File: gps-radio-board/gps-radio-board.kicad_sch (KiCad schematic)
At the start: 42 parts, among them J1 SMA, J2 SMA, J3 USB_C_Receptacle_USB2.0_16P, J4 JST_BATT, J5 Conn_01x04, J6 Conn_01x04, J7 Conn_01x04, U1 ESP32-C6-MINI-1U-H4, U4 AP2112K-3.3, U5 MAX-M10N, U6 MCP73831, U7 AP2112K-3.3

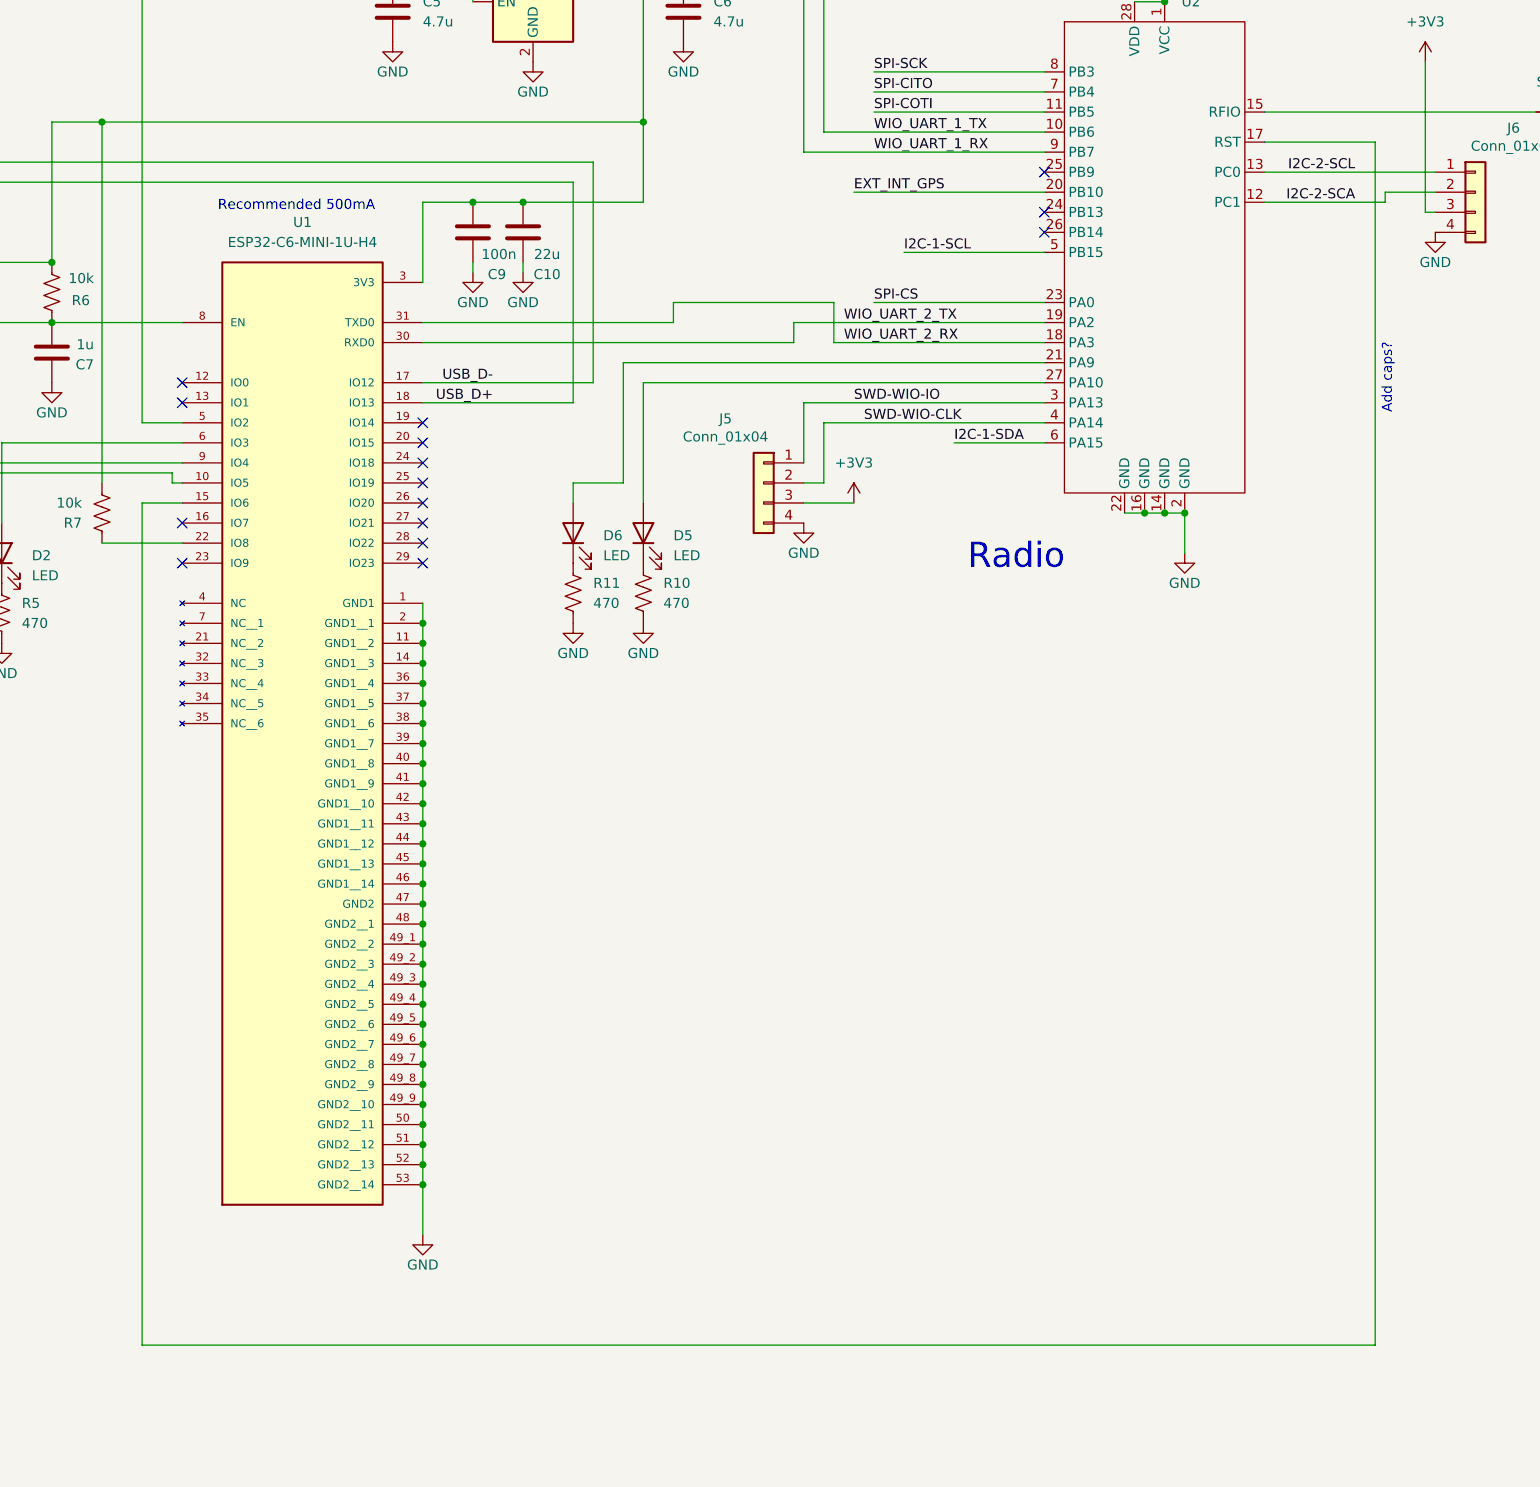
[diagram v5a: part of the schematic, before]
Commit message: Add 3d models for MCUs
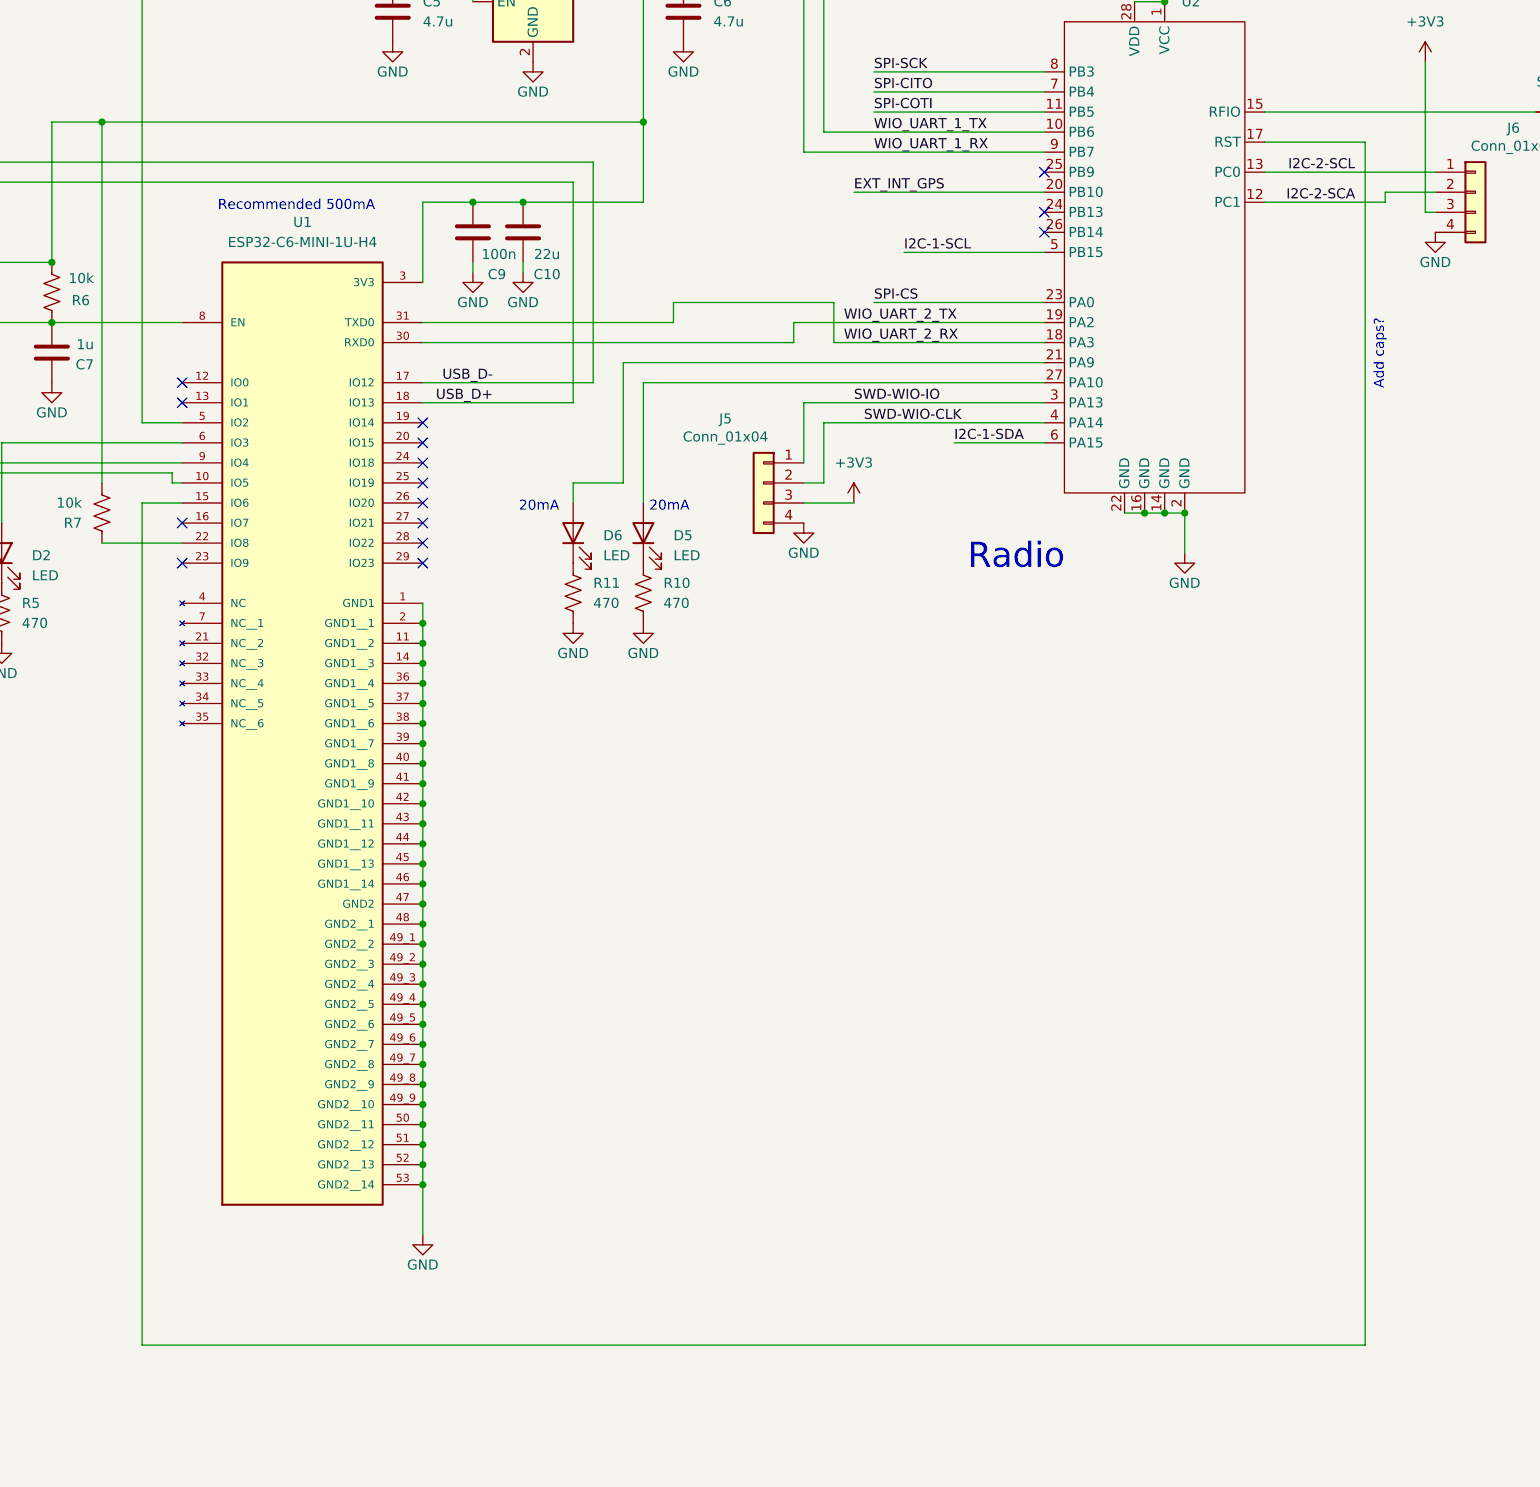
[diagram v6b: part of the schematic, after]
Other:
- note added: "20mA"
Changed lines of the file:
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@@
+		)
+	)
+	(text "20mA"
+		(exclude_from_sim no)
+		(at 558.292 366.268 0)
+		(effects
+			(font
+				(size 1.27 1.27)
+			)
 		)
 	)
@@
 	(text "Add caps?"
 		(exclude_from_sim no)
-		(at 665.734 350.012 90)
+		(at 664.718 346.964 90)
 		(effects
 			(font
@@
 		)
 	)
+	(text "20mA"
+		(exclude_from_sim no)
+		(at 574.802 366.268 0)
+		(effects
+			(font
+				(size 1.27 1.27)
+			)
+		)
+	)
 	(junction
 		(at 543.56 388.62)
@@
 	(wire
 		(pts
-			(xy 664.21 472.44) (xy 664.21 320.04)
+			(xy 662.94 472.44) (xy 662.94 320.04)
 		)
 		(stroke
@@
 	(wire
 		(pts
-			(xy 508 472.44) (xy 664.21 472.44)
+			(xy 508 472.44) (xy 662.94 472.44)
 		)
 		(stroke
@@
 	(wire
 		(pts
-			(xy 664.21 320.04) (xy 650.24 320.04)
-		)
-		(stroke
+			(xy 662.94 320.04) (xy 650.24 320.04)
+		)
+		(stroke

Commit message: Add active gps antenna circuit
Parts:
- added C13, C14: 100n, Capacitor_SMD:C_0603_1608Metric_Pad1.08x0.95mm_HandSolder, symbol Device:C
- added C15: 1u, Capacitor_SMD:C_0603_1608Metric_Pad1.08x0.95mm_HandSolder, symbol Device:C
- added C16: ?, Capacitor_SMD:C_0603_1608Metric_Pad1.08x0.95mm_HandSolder, symbol Device:C
- added L1: ?, Inductor_SMD:L_0603_1608Metric_Pad1.05x0.95mm_HandSolder, symbol Device:L
- added R12: 0, Resistor_SMD:R_0603_1608Metric_Pad0.98x0.95mm_HandSolder, symbol Device:R_US
- added R13, R14: 100k, Resistor_SMD:R_0603_1608Metric_Pad0.98x0.95mm_HandSolder, symbol Device:R_US
- added R15: 10, Resistor_SMD:R_0603_1608Metric_Pad0.98x0.95mm_HandSolder, symbol Device:R_US
- added U3: SiP32431DR3, Package_TO_SOT_SMD:SOT-363_SC-70-6, symbol Power_Management:SiP32431DR3
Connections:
- net +3V3: now also R12.2
- net GND: now also C13.2, C14.2, C15.1, C16.1, R14.1, U3.2 (GND), U3.5 (GND)
- net at C4.1, C5.1, D3.1 (K)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: now also R13.2
- net at J2.1 (In), U5.11 (RF_IN): now also L1.1
- net at U5.13 (LNA_EN): now also U5.14 (VCC_RF), R12.1, R14.2, U3.3 (ON)
- net at U1.5 (IO2), U4.3 (EN): now also R13.1
- net at U1.15 (IO6), U2.17 (RST): now also C13.1
- new net: C16.2, L1.2, R15.2
- new net: C15.2, U3.4 (IN)
- new net: C14.1, R15.1, U3.1 (OUT)
- no-connect marks 24 -> 22
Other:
- note added: "<-Connect if backup supply is wanted"
- note removed: "\/-Connect if backup supply is wanted"
- moved on the sheet: C1, C10, C11, C12, C2, C3, C4, C5, C6, C7, C8, C9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

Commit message: Routing, mostly finished
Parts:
- removed C2: 100n, Capacitor_SMD:C_0603_1608Metric_Pad1.08x0.95mm_HandSolder, symbol Device:C
- removed C3: 10u, Capacitor_SMD:C_0603_1608Metric_Pad1.08x0.95mm_HandSolder, symbol Device:C
- removed R12: 0, Resistor_SMD:R_0603_1608Metric_Pad0.98x0.95mm_HandSolder, symbol Device:R_US
- added BOOT1, GND1: TP2, TestPoint:TestPoint_Pad_1.0x1.0mm, symbol Connector:TestPoint
- added C17: 10u, Capacitor_SMD:C_0603_1608Metric_Pad1.08x0.95mm_HandSolder, symbol Device:C
- added C18: 4.7u, Capacitor_SMD:C_0603_1608Metric_Pad1.08x0.95mm_HandSolder, symbol Device:C
- added C19: 100n, Capacitor_SMD:C_0603_1608Metric_Pad1.08x0.95mm_HandSolder, symbol Device:C
- added EN1, EN2: ESP_EN, TestPoint:TestPoint_Pad_1.0x1.0mm, symbol Connector:TestPoint
- added J8: DM3CS-SF, Connector_Card:microSD_HC_Hirose_DM3D-SF, symbol 2026-05-05_06-59-55:DM3CS-SF
- added R16, R17, R18, R19: 10k, Resistor_SMD:R_0603_1608Metric_Pad0.98x0.95mm_HandSolder, symbol Device:R_US
- C16: value ? -> 10n
- L1: value ? -> 27n; footprint Inductor_SMD:L_0603_1608Metric_Pad1.05x0.95mm_HandSolder -> Inductor_SMD:L_0402_1005Metric_Pad0.77x0.64mm_HandSolder
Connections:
- net +3V3: now also C17.2, C18.1, C19.1, J8.4 (VDD), R16.2, R17.2, R18.2, R19.1
- net GND: now also C17.1, C18.2, C19.2, EN1.1, GND1.1, J8.10 (GND1), J8.6 (VSS), J8.SH
- net SPI-CITO: now also J8.7 (DAT0), R18.1
- net SPI-COTI: now also J8.3 (CMD), R17.1
- net SPI-CS: now also J8.2 (CD/DAT3), R16.1
- net SPI-SCK: now also J8.5 (CLK), R19.2
- net at C7.2, C8.1, R6.1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: now also EN2.1
- net at C15.2, U3.4 (IN): now also U5.14 (VCC_RF)
- net at R14.2, U3.3 (ON), U5.13 (LNA_EN): no longer U5.14 (VCC_RF)
- net at U1.23 (IO9): now also BOOT1.1
- no-connect marks 22 -> 24
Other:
- note added: "SD Card"
- note removed: "Add caps?"
